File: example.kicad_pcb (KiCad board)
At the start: 2 copper layers, 127 x 101.6 mm, 12 parts, among them P1 CONN_01X03, P3 CONN_01X06, P4 CONN_01X01, P5 CONN_01X20, P6 CONN_01X12, P7 CONN_01X16, P8 CONN_01X09, P9 CONN_01X04

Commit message: Saving PCB.
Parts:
- removed P5: CONN_01X20, Socket_Strips:Socket_Strip_Straight_1x20
- moved P8 21.7 mm to (186.7, 54.6), turned to 180 degrees
- moved P3 19.1 mm to (130.8, 82.5)
- moved R2 16.5 mm to (123.2, 78.7)
- moved P1 13.9 mm to (128.9, 69.8), turned to 0 degrees
- moved R1 12.6 mm to (139.1, 79.4), turned to 270 degrees
- moved P4 11.4 mm to (138.4, 69.8)
- moved G*** 2.84 mm to (213.4, 95.2)
- moved G*** 1.91 mm to (152.4, 125.1)
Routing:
- net /USB: track 146.5 -> 171.3 mm
- net /3V3: track 63.4 -> 87.0 mm
- net /GPS_TX: track 22.0 -> 42.7 mm
- net /GPS_RX: track 17.3 -> 32.2 mm
- net /BAT: track 23.6 -> 12.6 mm
- net GND: track 152.7 -> 145.6 mm, vias 0 -> 1
- net Net-(P3-Pad6): track 11.2 -> 7.77 mm
- net Net-(P4-Pad1): track 6.57 -> 5.13 mm

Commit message: Some rename/cleanup before pushing to github.
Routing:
- net /USB: track 171.3 -> 342.5 mm
- net /3V3: track 87.0 -> 174.0 mm
- net GND: track 145.6 -> 220.1 mm
- net /GPS_TX: track 42.7 -> 86.0 mm
- net /GPS_RX: track 32.2 -> 63.9 mm
- net /RB_TX: track 31.5 -> 62.8 mm
- net /RB_RX: track 27.1 -> 54.1 mm
- net /BAT: track 12.6 -> 25.0 mm
- net Net-(P3-Pad6): track 7.77 -> 15.5 mm
- net Net-(P4-Pad1): track 5.13 -> 10.0 mm

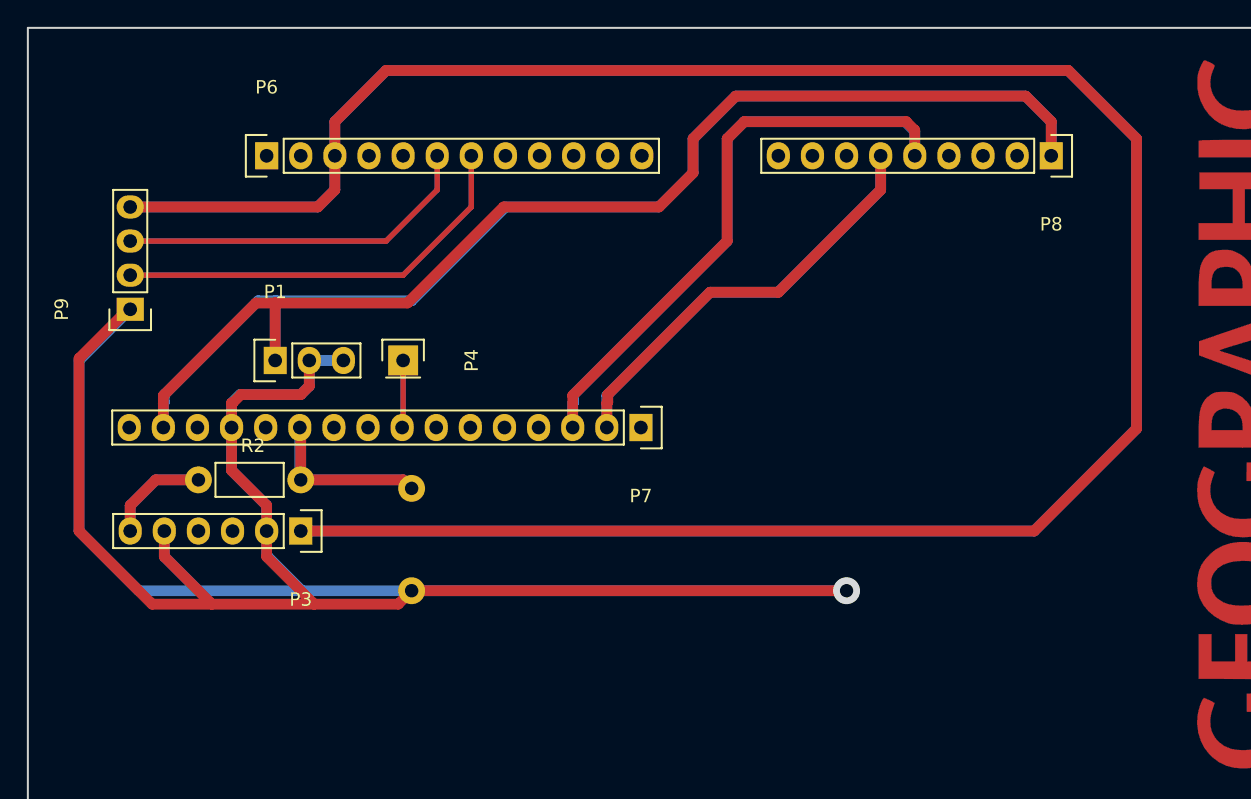
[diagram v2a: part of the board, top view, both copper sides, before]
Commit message: Adjust for wifi board for April demo.
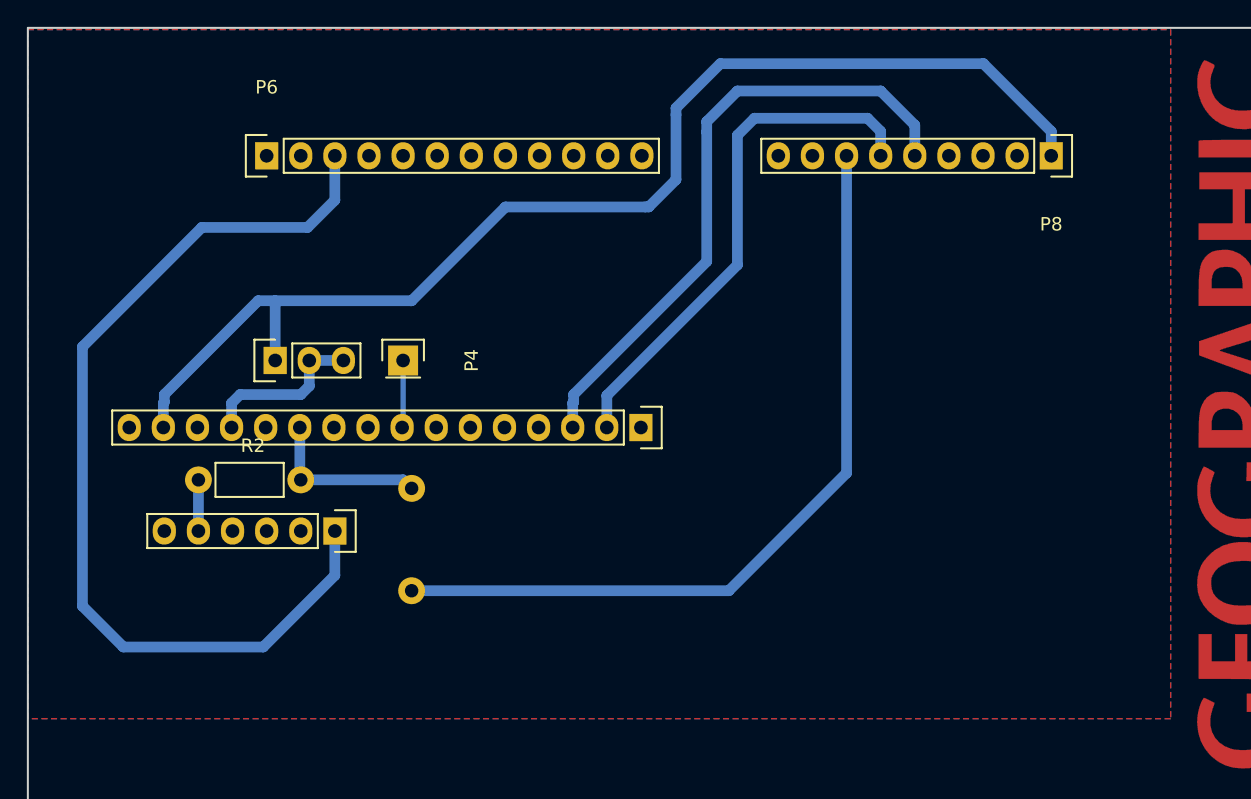
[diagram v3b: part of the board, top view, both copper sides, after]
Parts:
- removed P9: CONN_01X04, Socket_Strips:Socket_Strip_Straight_1x04
- moved P3 2.54 mm to (133.3, 82.5)
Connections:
- net /USB renamed /LOAD
- P3 pad 5: GND -> Net-(P3-Pad5)
- P3 pad 6: Net-(P3-Pad6) -> GND
- P6 pad 6: /RB_RX -> (no net)
- P6 pad 7: /RB_TX -> (no net)
- R2 pad 1: Net-(P3-Pad6) -> Net-(P3-Pad5)
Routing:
- net /LOAD: track 342.5 -> 71.5 mm
- net GND: track 220.1 -> 72.2 mm, vias 1 -> 0
- net /3V3: track 174.0 -> 90.2 mm
- net /RB_TX: track 62.8 -> 0.00 mm
- net /RB_RX: track 54.1 -> 0.00 mm
- net /GPS_TX: track 86.0 -> 46.7 mm
- net /GPS_RX: track 63.9 -> 39.2 mm
- net Net-(P3-Pad6): track 15.5 -> 0.00 mm
- net /BAT: track 25.0 -> 12.4 mm
- net Net-(P4-Pad1): track 10.0 -> 5.02 mm
- net Net-(P3-Pad5): track 0.00 -> 3.81 mm
- added copper zone on B.Cu, net GND
- added copper zone on F.Cu, net GND

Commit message: Add some LEDs for status indicators.
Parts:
- added D1: LED, Diodes_ThroughHole:D_T-1_P2.54mm_Vertical_AnodeUp, F.Cu at (112.8, 47.8)
- added D2: LED, Diodes_ThroughHole:D_T-1_P2.54mm_Vertical_AnodeUp, F.Cu at (129.3, 47.9)
- added D3: LED, Diodes_ThroughHole:D_T-1_P2.54mm_Vertical_AnodeUp, F.Cu at (145.5, 47.9)
- added R3: R, Resistors_ThroughHole:R_Axial_DIN0207_L6.3mm_D2.5mm_P7.62mm_Horizontal, F.Cu at (125.8, 47.8)
- added R4: R, Resistors_ThroughHole:R_Axial_DIN0207_L6.3mm_D2.5mm_P7.62mm_Horizontal, F.Cu at (142.2, 47.9)
- added R5: R, Resistors_ThroughHole:R_Axial_DIN0207_L6.3mm_D2.5mm_P7.62mm_Horizontal, F.Cu at (158.5, 47.9)
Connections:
- P6 pad 5: (no net) -> Net-(P6-Pad5)
- P6 pad 6: (no net) -> Net-(P6-Pad6)
- P6 pad 7: (no net) -> Net-(P6-Pad7)
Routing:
- net Net-(P6-Pad7): track 0.00 -> 18.8 mm
- net Net-(P6-Pad5): track 0.00 -> 18.0 mm
- net Net-(P6-Pad6): track 0.00 -> 7.24 mm
- net Net-(D2-Pad2): track 0.00 -> 2.80 mm
- net Net-(D3-Pad2): track 0.00 -> 2.79 mm
- net Net-(D1-Pad2): track 0.00 -> 2.79 mm

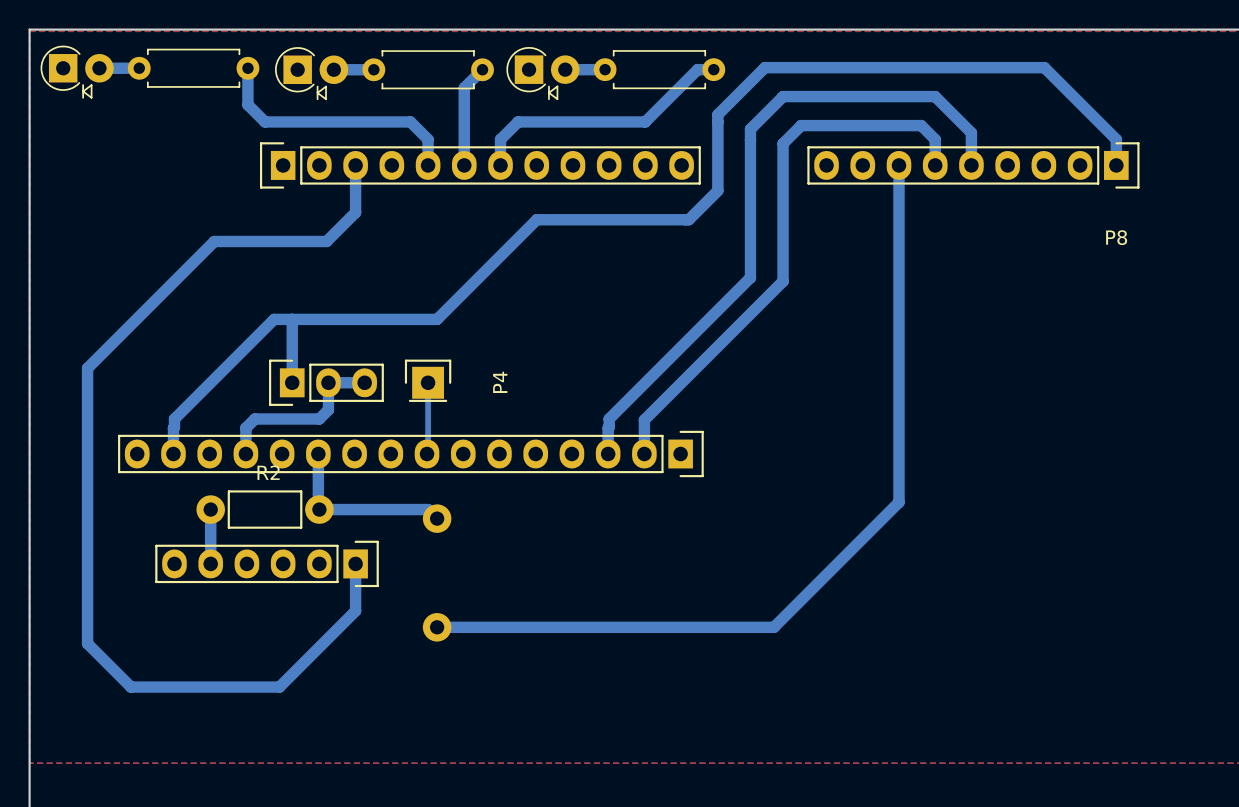
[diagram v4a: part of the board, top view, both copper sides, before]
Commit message: Nudge circuit inwards.
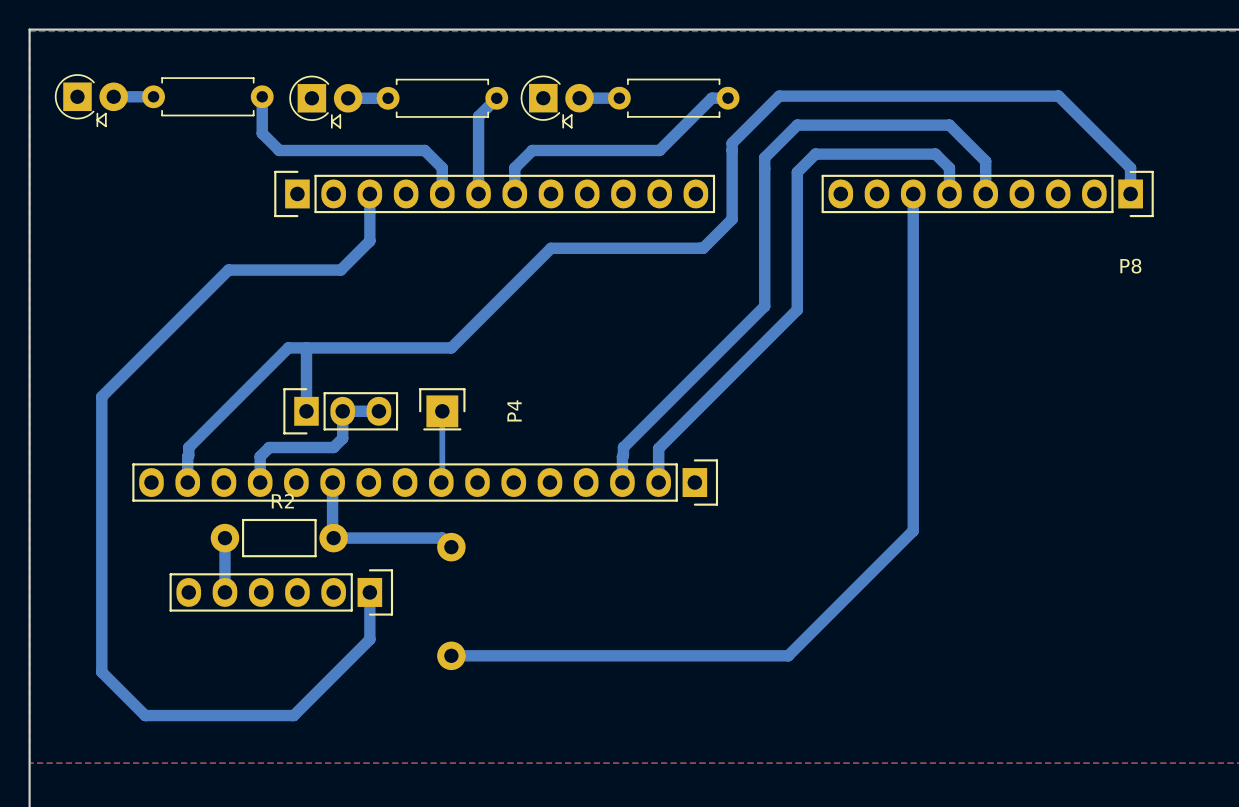
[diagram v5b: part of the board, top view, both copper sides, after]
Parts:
- moved D1 2.24 mm to (113.8, 49.8)
- moved D2 2.24 mm to (130.3, 49.9)
- moved D3 2.24 mm to (146.5, 49.9)
- moved P1 2.24 mm to (129.9, 71.8)
- moved P3 2.24 mm to (134.3, 84.5)
- moved P4 2.24 mm to (139.4, 71.8)
- moved P6 2.24 mm to (129.3, 56.6)
- moved P7 2.24 mm to (157.1, 76.8)
- moved P8 2.24 mm to (187.7, 56.6)
- moved R1 2.24 mm to (140.1, 81.4)
- moved R2 2.24 mm to (124.2, 80.7)
- moved R3 2.24 mm to (126.8, 49.8)
- moved R4 2.24 mm to (143.2, 49.9)
- moved R5 2.24 mm to (159.5, 49.9)
